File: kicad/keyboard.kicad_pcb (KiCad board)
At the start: 2 copper layers, 266 x 95 mm, 74 parts, among them SW1 SW_MEC_5G, SW10 SW_MEC_5G, SW11 SW_MEC_5G, SW12 SW_MEC_5G, SW13 SW_MEC_5G, SW14 SW_MEC_5G, SW15 SW_MEC_5G, SW16 SW_MEC_5G, SW17 SW_MEC_5G, SW18 SW_MEC_5G, SW19 SW_MEC_5G, SW2 SW_MEC_5G, SW20 SW_MEC_5G, SW21 SW_MEC_5G, SW22 SW_MEC_5G, SW23 SW_MEC_5G, SW24 SW_MEC_5G, SW25 SW_MEC_5G, SW26 SW_MEC_5G, SW27 SW_MEC_5G, SW28 SW_MEC_5G, SW29 SW_MEC_5G, SW3 SW_MEC_5G, SW30 SW_MEC_5G, SW31 SW_MEC_5G, SW32 SW_MEC_5G, SW33 SW_MEC_5G, SW34 SW_MEC_5G, SW35 SW_MEC_5G, SW36 SW_MEC_5G, SW37 SW_MEC_5G, SW38 SW_MEC_5G, SW39 SW_MEC_5G, SW4 SW_MEC_5G, SW40 SW_MEC_5G, SW41 SW_MEC_5G, SW42 SW_MEC_5G, SW43 SW_MEC_5G, SW44 SW_MEC_5G, SW45 SW_MEC_5G, SW46 SW_MEC_5G, SW47 SW_MEC_5G, SW48 SW_MEC_5G, SW49 SW_MEC_5G, SW5 SW_MEC_5G, SW50 SW_MEC_5G, SW51 SW_MEC_5G, SW52 SW_MEC_5G, SW53 SW_MEC_5G, SW54 SW_MEC_5G, SW55 SW_MEC_5G, SW56 SW_MEC_5G, SW57 SW_MEC_5G, SW58 SW_MEC_5G, SW59 SW_MEC_5G, SW6 SW_MEC_5G, SW60 SW_MEC_5G, SW7 SW_MEC_5G, SW8 SW_MEC_5G, SW9 SW_MEC_5G, U1 MCP23017-E/SO, U2 MCP23017-E/SO, U3 MCP23017-E/SO, U4 MCP23017-E/SO

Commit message: Started tracing signals, added jlcpcb settings
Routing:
- net /SW12: track 0.00 -> 11.6 mm
- net /SW16: track 0.00 -> 11.6 mm
- net /SW5: track 0.00 -> 11.6 mm
- net /SW19: track 0.00 -> 11.6 mm
- net /SW2: track 0.00 -> 11.5 mm
- net /SW48: track 0.00 -> 11.5 mm
- net /SW20: track 0.00 -> 11.5 mm
- net /SW4: track 0.00 -> 11.5 mm
- net /SW50: track 0.00 -> 11.5 mm
- net /SW52: track 0.00 -> 11.5 mm
- net /SW60: track 0.00 -> 11.5 mm
- net /SW17: track 0.00 -> 11.5 mm
- net /SW42: track 0.00 -> 11.5 mm
- net /SW56: track 0.00 -> 11.5 mm
- net /SW28: track 0.00 -> 11.4 mm
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
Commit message: wip tracing
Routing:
- net /3v3: track 0.00 -> 93.9 mm, vias 0 -> 4
- net /SW33: track 0.00 -> 12.9 mm
- net /SW29: track 0.00 -> 12.8 mm
- net /SW47: track 0.00 -> 11.9 mm
- net /SW43: track 0.00 -> 11.8 mm
- net /SW35: track 0.00 -> 11.7 mm
- net /SW53: track 0.00 -> 11.4 mm
- net /SW51: track 0.00 -> 11.4 mm
- net /SW49: track 0.00 -> 11.4 mm
- net /SW41: track 0.00 -> 11.4 mm
- net /SW39: track 0.00 -> 11.4 mm
- net /SW37: track 0.00 -> 11.4 mm
- net /SW59: track 0.00 -> 11.4 mm
- net /SW57: track 0.00 -> 11.4 mm
- net /SW55: track 0.00 -> 11.4 mm
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- added copper zone on B.Cu, net /GND

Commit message: WIP tracing
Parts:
- A1: value TINY2040 -> TINY2040-pimoroni-boards
- moved R4 24.4 mm to (207.2, 129.2)
- moved R1 1.18 mm to (222.8, 106.0)
- moved R5 1.16 mm to (227.2, 105.9)
- moved R9 0.26 mm to (227.4, 157.3), turned to -90 degrees
- moved R8 0.24 mm to (207.4, 157.1), turned to -90 degrees
- moved R7 0.12 mm to (222.5, 157.2)
- turned R6 to 90 degrees
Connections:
- U1 pad 21: /SW2 -> /SW4
- U1 pad 22: /SW4 -> /SW2
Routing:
- net /SW23: track 10.9 -> 175.2 mm
- net /SW59: track 11.4 -> 164.7 mm
- net /SW21: track 11.3 -> 158.3 mm
- net /SW34: track 11.4 -> 156.1 mm
- net /SW6: track 11.3 -> 149.4 mm
- net /SW57: track 11.4 -> 147.8 mm
- net /SW11: track 11.3 -> 142.0 mm
- net /SW46: track 11.4 -> 140.5 mm
- net /SW19: track 11.6 -> 140.2 mm
- net /SW36: track 11.4 -> 135.2 mm
- net /SW35: track 11.7 -> 132.0 mm
- net /SW55: track 11.4 -> 131.1 mm
- net /SW8: track 11.4 -> 130.6 mm
- net /SW47: track 11.9 -> 130.4 mm
- net /SW31: track 11.0 -> 124.6 mm
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
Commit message: WIP tracing
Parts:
- moved R4 70.3 mm to (214.6, 59.2)
- moved R1 64.4 mm to (222.3, 41.5)
- moved R5 63.8 mm to (228.8, 42.1)
- moved U1 62.7 mm to (204.1, 54.6)
- moved U2 62.2 mm to (228.5, 55.1)
- moved R6 43.4 mm to (203.8, 200.6)
- moved R8 42.9 mm to (197.3, 198.8)
- moved R7 39.7 mm to (241.1, 192.3)
- moved U3 38.6 mm to (201.6, 184.2)
- moved U4 38.0 mm to (225.6, 183.8)
- moved R9 33.3 mm to (233.2, 190.1)
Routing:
- net /SW59: track 164.7 -> 9.76 mm
- net /SW57: track 147.8 -> 11.4 mm
- net /3v3: track 152.9 -> 27.7 mm, vias 4 -> 0
- net /SW55: track 131.1 -> 11.4 mm
- net /SW47: track 130.4 -> 11.0 mm
- net /SW53: track 113.0 -> 11.4 mm
- net /SW45: track 111.5 -> 11.1 mm
- net /SW29: track 106.9 -> 13.1 mm
- net /SW43: track 93.7 -> 12.4 mm
- net /SW51: track 90.7 -> 11.4 mm
- net /SW27: track 85.6 -> 11.2 mm
- net /SW49: track 73.1 -> 0.00 mm
- net /SW41: track 74.2 -> 11.7 mm
- net /SW17: track 121.0 -> 63.1 mm
- net /SW19: track 140.2 -> 82.9 mm
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
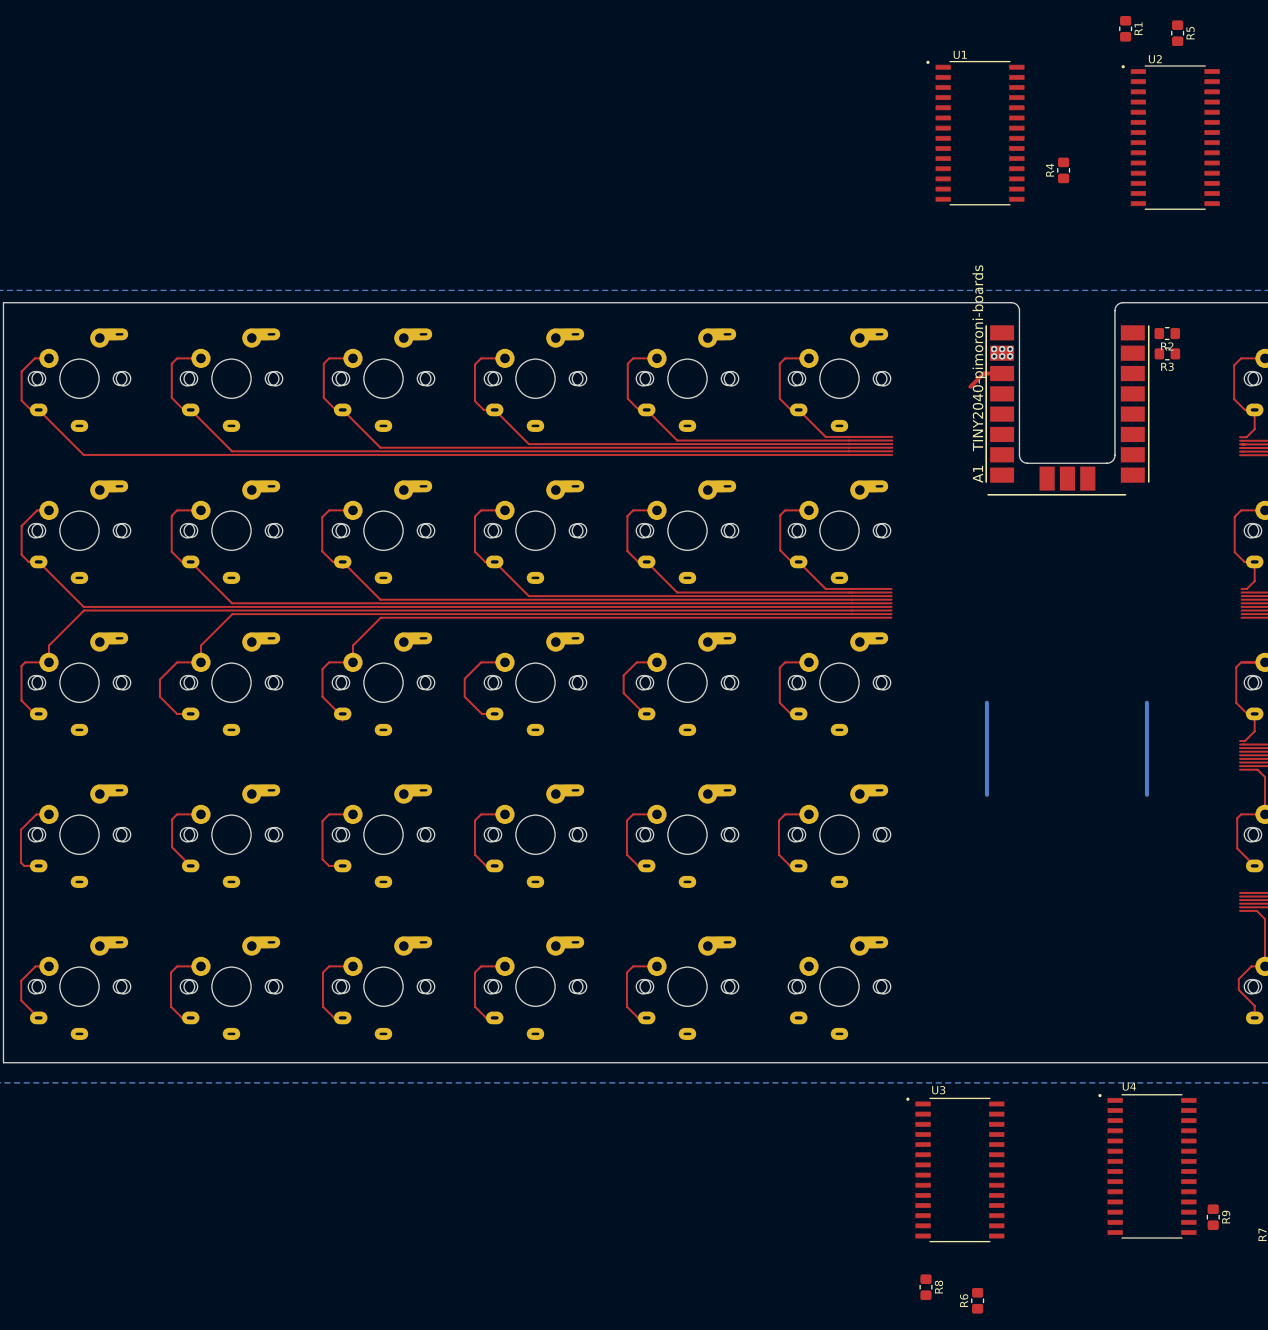
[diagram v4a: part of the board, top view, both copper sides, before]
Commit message: Reordered switch pins and re-traced
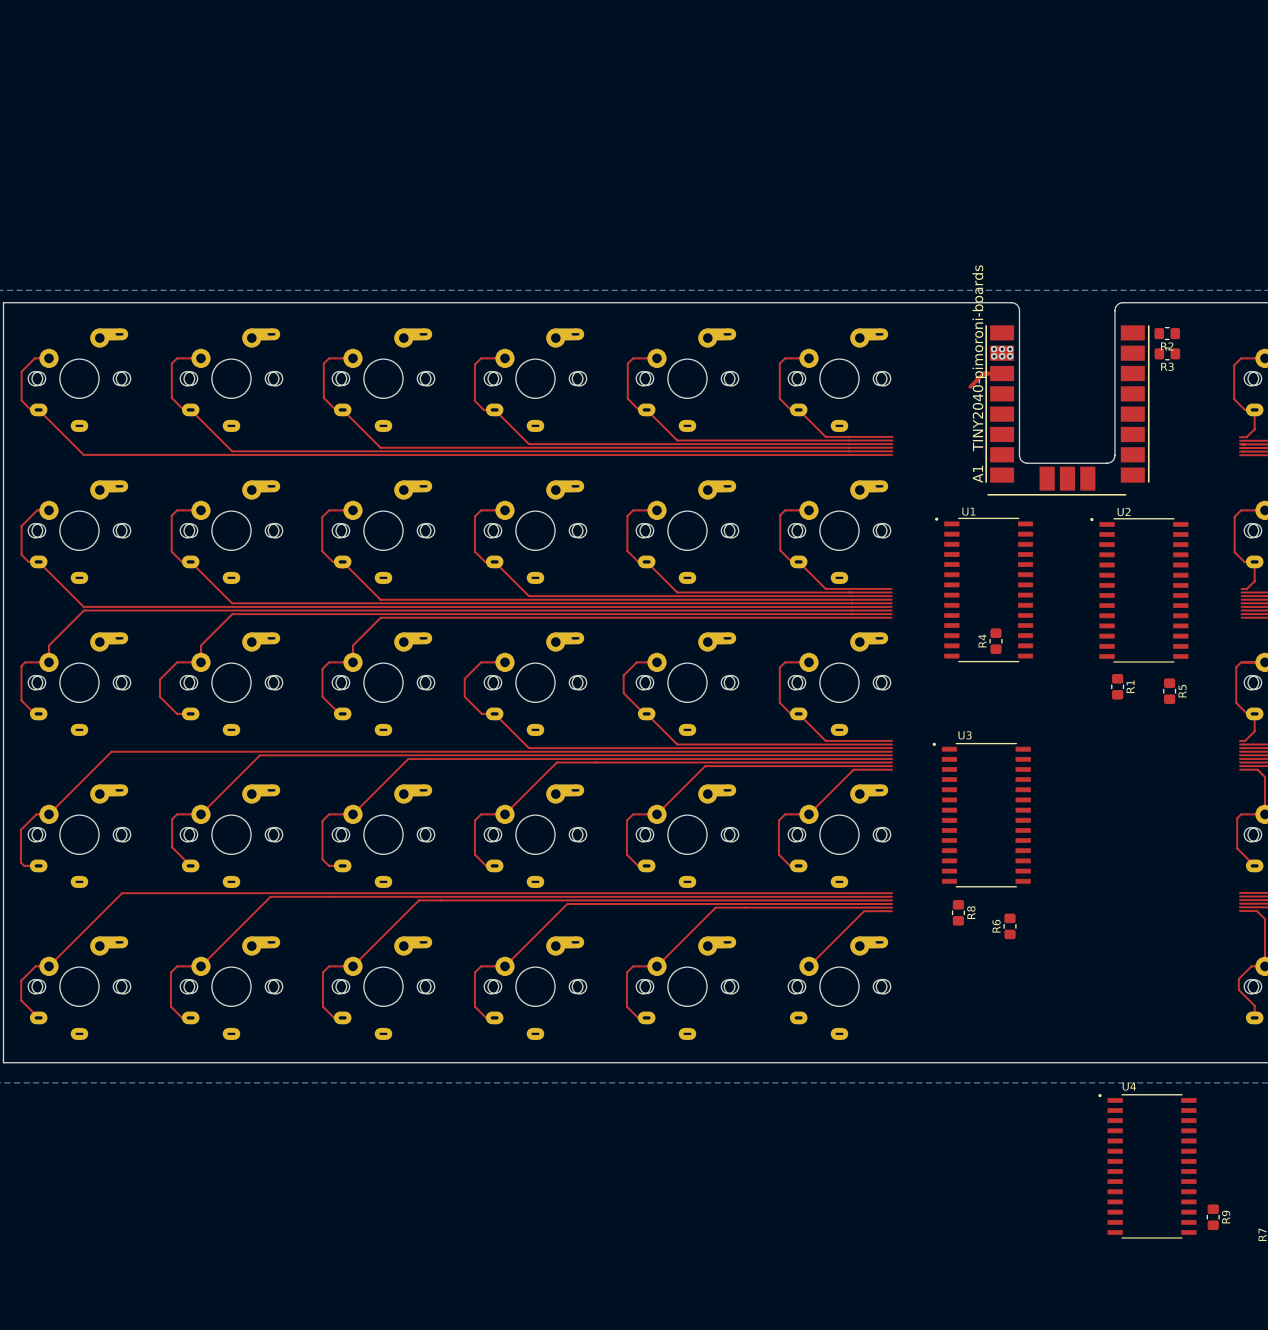
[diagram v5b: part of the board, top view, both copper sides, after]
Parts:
- moved R1 82.3 mm to (221.3, 123.8)
- moved R5 82.3 mm to (227.8, 124.3)
- moved R4 59.5 mm to (206.1, 118.1)
- moved U1 57.1 mm to (205.2, 111.7)
- moved U2 56.7 mm to (224.6, 111.8)
- moved R6 47.0 mm to (207.8, 153.8)
- moved R8 47.0 mm to (201.4, 152.1)
- moved U3 44.5 mm to (204.9, 139.8)
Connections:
- U1 pad 2: /SW3 -> /SW5
- U1 pad 21: /SW4 -> unconnected-(U1-Pad21)
- U1 pad 22: /SW2 -> /SW33
- U1 pad 23: /SW6 -> /SW23
- U1 pad 24: /SW8 -> /SW19
- U1 pad 25: /SW10 -> /SW15
- U1 pad 26: /SW12 -> /SW11
- U1 pad 27: /SW14 -> /SW7
- U1 pad 28: /SW16 -> /SW3
- U1 pad 3: /SW5 -> /SW9
- U1 pad 4: /SW7 -> /SW13
- U1 pad 5: /SW9 -> /SW17
- U1 pad 6: /SW11 -> /SW21
- U1 pad 7: /SW13 -> /SW35
- U1 pad 8: /SW15 -> /SW31
- U2 pad 1: /SW17 -> unconnected-(U2-Pad1)
- U2 pad 2: /SW19 -> unconnected-(U2-Pad2)
- U2 pad 3: /SW21 -> unconnected-(U2-Pad3)
- U2 pad 4: /SW23 -> unconnected-(U2-Pad4)
- U2 pad 5: /SW25 -> unconnected-(U2-Pad5)
- U2 pad 6: /SW27 -> unconnected-(U2-Pad6)
- U2 pad 7: /SW29 -> unconnected-(U2-Pad7)
- U2 pad 8: /SW31 -> unconnected-(U2-Pad8)
- U3 pad 1: /SW33 -> /SW25
- U3 pad 2: /SW35 -> /SW29
- U3 pad 21: /SW34 -> unconnected-(U3-Pad21)
- U3 pad 22: /SW36 -> /SW51
- U3 pad 23: /SW38 -> /SW55
- U3 pad 24: /SW40 -> /SW59
- U3 pad 25: /SW42 -> /SW39
- U3 pad 26: /SW44 -> /SW43
- U3 pad 27: /SW46 -> /SW47
- U3 pad 28: /SW48 -> /SW27
- U3 pad 3: /SW37 -> /SW45
- U3 pad 4: /SW39 -> /SW41
- U3 pad 5: /SW41 -> /SW37
- U3 pad 6: /SW43 -> /SW57
- U3 pad 7: /SW45 -> /SW53
- U3 pad 8: /SW47 -> /SW49
- U4 pad 1: /SW49 -> unconnected-(U4-Pad1)
- U4 pad 2: /SW51 -> unconnected-(U4-Pad2)
- U4 pad 3: /SW53 -> unconnected-(U4-Pad3)
- U4 pad 4: /SW55 -> unconnected-(U4-Pad4)
- U4 pad 5: /SW57 -> unconnected-(U4-Pad5)
- U4 pad 6: /SW59 -> unconnected-(U4-Pad6)
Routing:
- net /SW59: track 9.76 -> 118.9 mm
- net /SW47: track 11.0 -> 119.7 mm
- net /SW57: track 11.4 -> 101.4 mm
- net /SW45: track 11.1 -> 100.5 mm
- net /SW55: track 11.4 -> 82.2 mm
- net /SW43: track 12.4 -> 82.6 mm
- net /SW53: track 11.4 -> 63.0 mm
- net /SW29: track 13.1 -> 64.5 mm
- net /SW41: track 11.7 -> 62.8 mm
- net /SW51: track 11.4 -> 43.8 mm
- net /SW27: track 11.2 -> 43.4 mm
- net /SW39: track 11.4 -> 43.3 mm
- net /3v3: track 27.7 -> 4.65 mm
- net /SW49: track 0.00 -> 13.2 mm
- net /SW25: track 11.3 -> 24.3 mm
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
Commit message: Reordered switch pins and re-traced
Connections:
- U2 pad 1: unconnected-(U2-Pad1) -> /SW14
- U2 pad 2: unconnected-(U2-Pad2) -> /SW10
- U2 pad 21: /SW18 -> /SW44
- U2 pad 22: /SW20 -> /SW40
- U2 pad 23: /SW22 -> /SW36
- U2 pad 24: /SW24 -> /SW20
- U2 pad 25: /SW26 -> /SW24
- U2 pad 26: /SW28 -> /SW8
- U2 pad 27: /SW30 -> /SW12
- U2 pad 28: /SW32 -> /SW16
- U2 pad 3: unconnected-(U2-Pad3) -> /SW6
- U2 pad 4: unconnected-(U2-Pad4) -> /SW22
- U2 pad 5: unconnected-(U2-Pad5) -> /SW34
- U2 pad 6: unconnected-(U2-Pad6) -> /SW38
- U2 pad 7: unconnected-(U2-Pad7) -> /SW42
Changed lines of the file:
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@@
   (net 97 "unconnected-(U4-Pad8)")
   (net 98 "unconnected-(U4-Pad7)")
-  (net 99 "unconnected-(U2-Pad1)")
-  (net 100 "unconnected-(U2-Pad2)")
-  (net 101 "unconnected-(U1-Pad21)")
-  (net 102 "unconnected-(U2-Pad3)")
-  (net 103 "unconnected-(U2-Pad4)")
-  (net 104 "unconnected-(U2-Pad8)")
-  (net 105 "unconnected-(U2-Pad5)")
-  (net 106 "unconnected-(U2-Pad6)")
-  (net 107 "unconnected-(U2-Pad7)")
-  (net 108 "unconnected-(U3-Pad21)")
-  (net 109 "unconnected-(U4-Pad1)")
-  (net 110 "unconnected-(U4-Pad2)")
-  (net 111 "unconnected-(U4-Pad3)")
-  (net 112 "unconnected-(U4-Pad4)")
-  (net 113 "unconnected-(U4-Pad5)")
-  (net 114 "unconnected-(U4-Pad6)")
+  (net 99 "unconnected-(U1-Pad21)")
+  (net 100 "unconnected-(U2-Pad8)")
+  (net 101 "unconnected-(U3-Pad21)")
+  (net 102 "unconnected-(U4-Pad1)")
+  (net 103 "unconnected-(U4-Pad2)")
+  (net 104 "unconnected-(U4-Pad3)")
+  (net 105 "unconnected-(U4-Pad4)")
+  (net 106 "unconnected-(U4-Pad5)")
+  (net 107 "unconnected-(U4-Pad6)")
   (footprint "footprints:CherryMX_ChocV2_1u" (layer "F.Cu")
     (at 338.532 85.29)
@@
       (net 91 "unconnected-(U3-Pad20)") (pinfunction "INTA") (pintype "output+no_connect"))
     (pad "21" smd roundrect locked (at 4.605 0.635) (size 1.9 0.6) (layers "F.Cu" "F.Paste" "F.Mask") (roundrect_rratio 0.07)
-      (net 108 "unconnected-(U3-Pad21)") (pinfunction "GPA0") (pintype "bidirectional"))
+      (net 101 "unconnected-(U3-Pad21)") (pinfunction "GPA0") (pintype "bidirectional"))
     (pad "22" smd roundrect locked (at 4.605 -0.635) (size 1.9 0.6) (layers "F.Cu" "F.Paste" "F.Mask") (roundrect_rratio 0.07)
       (net 77 "/SW51") (pinfunction "GPA1") (pintype "bidirectional"))
@@
     (fp_circle (center -6.505 -8.855) (end -6.405 -8.855) (layer "F.Fab") (width 0.2) (fill none))
     (pad "1" smd roundrect locked (at -4.605 -8.255) (size 1.9 0.6) (layers "F.Cu" "F.Paste" "F.Mask") (roundrect_rratio 0.07)
-      (net 109 "unconnected-(U4-Pad1)") (pinfunction "GPB0") (pintype "bidirectional"))
+      (net 102 "unconnected-(U4-Pad1)") (pinfunction "GPB0") (pintype "bidirectional"))
     (pad "2" smd roundrect locked (at -4.605 -6.985) (size 1.9 0.6) (layers "F.Cu" "F.Paste" "F.Mask") (roundrect_rratio 0.07)
-      (net 110 "unconnected-(U4-Pad2)") (pinfunction "GPB1") (pintype "bidirectional"))
+      (net 103 "unconnected-(U4-Pad2)") (pinfunction "GPB1") (pintype "bidirectional"))
     (pad "3" smd roundrect locked (at -4.605 -5.715) (size 1.9 0.6) (layers "F.Cu" "F.Paste" "F.Mask") (roundrect_rratio 0.07)
-      (net 111 "unconnected-(U4-Pad3)") (pinfunction "GPB2") (pintype "bidirectional"))
+      (net 104 "unconnected-(U4-Pad3)") (pinfunction "GPB2") (pintype "bidirectional"))
     (pad "4" smd roundrect locked (at -4.605 -4.445) (size 1.9 0.6) (layers "F.Cu" "F.Paste" "F.Mask") (roundrect_rratio 0.07)
-      (net 112 "unconnected-(U4-Pad4)") (pinfunction "GPB3") (pintype "bidirectional"))
+      (net 105 "unconnected-(U4-Pad4)") (pinfunction "GPB3") (pintype "bidirectional"))
     (pad "5" smd roundrect locked (at -4.605 -3.175) (size 1.9 0.6) (layers "F.Cu" "F.Paste" "F.Mask") (roundrect_rratio 0.07)
-      (net 113 "unconnected-(U4-Pad5)") (pinfunction "GPB4") (pintype "bidirectional"))
+      (net 106 "unconnected-(U4-Pad5)") (pinfunction "GPB4") (pintype "bidirectional"))
     (pad "6" smd roundrect locked (at -4.605 -1.905) (size 1.9 0.6) (layers "F.Cu" "F.Paste" "F.Mask") (roundrect_rratio 0.07)
-      (net 114 "unconnected-(U4-Pad6)") (pinfunction "GPB5") (pintype "bidirectional"))
+      (net 107 "unconnected-(U4-Pad6)") (pinfunction "GPB5") (pintype "bidirectional"))
     (pad "7" smd roundrect locked (at -4.605 -0.635) (size 1.9 0.6) (layers "F.Cu" "F.Paste" "F.Mask") (roundrect_rratio 0.07)
       (net 98 "unconnected-(U4-Pad7)") (pinfunction "GPB6") (pintype "bidirectional+no_connect"))
@@
       (net 87 "unconnected-(U1-Pad20)") (pinfunction "INTA") (pintype "output+no_connect"))
     (pad "21" smd roundrect locked (at 4.605 0.635) (size 1.9 0.6) (layers "F.Cu" "F.Paste" "F.Mask") (roundrect_rratio 0.07)
-      (net 101 "unconnected-(U1-Pad21)") (pinfunction "GPA0") (pintype "bidirectional"))
+      (net 99 "unconnected-(U1-Pad21)") (pinfunction "GPA0") (pintype "bidirectional"))
     (pad "22" smd roundrect locked (at 4.605 -0.635) (size 1.9 0.6) (layers "F.Cu" "F.Paste" "F.Mask") (roundrect_rratio 0.07)
       (net 59 "/SW33") (pinfunction "GPA1") (pintype "bidirectional"))
@@
     (fp_circle (center -6.505 -8.855) (end -6.405 -8.855) (layer "F.Fab") (width 0.2) (fill none))
     (pad "1" smd roundrect locked (at -4.605 -8.255) (size 1.9 0.6) (layers "F.Cu" "F.Paste" "F.Mask") (roundrect_rratio 0.07)
-      (net 99 "unconnected-(U2-Pad1)") (pinfunction "GPB0") (pintype "bidirectional"))
+      (net 40 "/SW14") (pinfunction "GPB0") (pintype "bidirectional"))
     (pad "2" smd roundrect locked (at -4.605 -6.985) (size 1.9 0.6) (layers "F.Cu" "F.Paste" "F.Mask") (roundrect_rratio 0.07)
-      (net 100 "unconnected-(U2-Pad2)") (pinfunction "GPB1") (pintype "bidirectional"))
+      (net 36 "/SW10") (pinfunction "GPB1") (pintype "bidirectional"))
     (pad "3" smd roundrect locked (at -4.605 -5.715) (size 1.9 0.6) (layers "F.Cu" "F.Paste" "F.Mask") (roundrect_rratio 0.07)
-      (net 102 "unconnected-(U2-Pad3)") (pinfunction "GPB2") (pintype "bidirectional"))
+      (net 32 "/SW6") (pinfunction "GPB2") (pintype "bidirectional"))
     (pad "4" smd roundrect locked (at -4.605 -4.445) (size 1.9 0.6) (layers "F.Cu" "F.Paste" "F.Mask") (roundrect_rratio 0.07)
-      (net 103 "unconnected-(U2-Pad4)") (pinfunction "GPB3") (pintype "bidirectional"))
+      (net 48 "/SW22") (pinfunction "GPB3") (pintype "bidirectional"))
     (pad "5" smd roundrect locked (at -4.605 -3.175) (size 1.9 0.6) (layers "F.Cu" "F.Paste" "F.Mask") (roundrect_rratio 0.07)
-      (net 105 "unconnected-(U2-Pad5)") (pinfunction "GPB4") (pintype "bidirectional"))
+      (net 60 "/SW34") (pinfunction "GPB4") (pintype "bidirectional"))
     (pad "6" smd roundrect locked (at -4.605 -1.905) (size 1.9 0.6) (layers "F.Cu" "F.Paste" "F.Mask") (roundrect_rratio 0.07)
-      (net 106 "unconnected-(U2-Pad6)") (pinfunction "GPB5") (pintype "bidirectional"))
+      (net 64 "/SW38") (pinfunction "GPB5") (pintype "bidirectional"))
     (pad "7" smd roundrect locked (at -4.605 -0.635) (size 1.9 0.6) (layers "F.Cu" "F.Paste" "F.Mask") (roundrect_rratio 0.07)
-      (net 107 "unconnected-(U2-Pad7)") (pinfunction "GPB6") (pintype "bidirectional"))
+      (net 68 "/SW42") (pinfunction "GPB6") (pintype "bidirectional"))
     (pad "8" smd roundrect locked (at -4.605 0.635) (size 1.9 0.6) (layers "F.Cu" "F.Paste" "F.Mask") (roundrect_rratio 0.07)
-      (net 104 "unconnected-(U2-Pad8)") (pinfunction "GPB7") (pintype "bidirectional"))
+      (net 100 "unconnected-(U2-Pad8)") (pinfunction "GPB7") (pintype "bidirectional"))
     (pad "9" smd roundrect locked (at -4.605 1.905) (size 1.9 0.6) (layers "F.Cu" "F.Paste" "F.Mask") (roundrect_rratio 0.07)
       (net 5 "/3v3") (pinfunction "VDD") (pintype "power_in"))
@@
       (net 89 "unconnected-(U2-Pad20)") (pinfunction "INTA") (pintype "output+no_connect"))
     (pad "21" smd roundrect locked (at 4.605 0.635) (size 1.9 0.6) (layers "F.Cu" "F.Paste" "F.Mask") (roundrect_rratio 0.07)
-      (net 44 "/SW18") (pinfunction "GPA0") (pintype "bidirectional"))
+      (net 70 "/SW44") (pinfunction "GPA0") (pintype "bidirectional"))
     (pad "22" smd roundrect locked (at 4.605 -0.635) (size 1.9 0.6) (layers "F.Cu" "F.Paste" "F.Mask") (roundrect_rratio 0.07)
-      (net 46 "/SW20") (pinfunction "GPA1") (pintype "bidirectional"))
+      (net 66 "/SW40") (pinfunction "GPA1") (pintype "bidirectional"))
     (pad "23" smd roundrect locked (at 4.605 -1.905) (size 1.9 0.6) (layers "F.Cu" "F.Paste" "F.Mask") (roundrect_rratio 0.07)
-      (net 48 "/SW22") (pinfunction "GPA2") (pintype "bidirectional"))
+      (net 62 "/SW36") (pinfunction "GPA2") (pintype "bidirectional"))
     (pad "24" smd roundrect locked (at 4.605 -3.175) (size 1.9 0.6) (layers "F.Cu" "F.Paste" "F.Mask") (roundrect_rratio 0.07)
-      (net 50 "/SW24") (pinfunction "GPA3") (pintype "bidirectional"))
+      (net 46 "/SW20") (pinfunction "GPA3") (pintype "bidirectional"))
     (pad "25" smd roundrect locked (at 4.605 -4.445) (size 1.9 0.6) (layers "F.Cu" "F.Paste" "F.Mask") (roundrect_rratio 0.07)
-      (net 52 "/SW26") (pinfunction "GPA4") (pintype "bidirectional"))
+      (net 50 "/SW24") (pinfunction "GPA4") (pintype "bidirectional"))
     (pad "26" smd roundrect locked (at 4.605 -5.715) (size 1.9 0.6) (layers "F.Cu" "F.Paste" "F.Mask") (roundrect_rratio 0.07)
-      (net 54 "/SW28") (pinfunction "GPA5") (pintype "bidirectional"))
+      (net 34 "/SW8") (pinfunction "GPA5") (pintype "bidirectional"))
     (pad "27" smd roundrect locked (at 4.605 -6.985) (size 1.9 0.6) (layers "F.Cu" "F.Paste" "F.Mask") (roundrect_rratio 0.07)
-      (net 56 "/SW30") (pinfunction "GPA6") (pintype "bidirectional"))
+      (net 38 "/SW12") (pinfunction "GPA6") (pintype "bidirectional"))
     (pad "28" smd roundrect locked (at 4.605 -8.255) (size 1.9 0.6) (layers "F.Cu" "F.Paste" "F.Mask") (roundrect_rratio 0.07)
-      (net 58 "/SW32") (pinfunction "GPA7") (pintype "bidirectional"))
-  )
-  (footprint "footprints:CherryMX_ChocV2_1u" (layer "F.Cu")
+      (net 42 "/SW16") (pinfunction "GPA7") (pintype "bidirectional"))
+  )
+  (footprint "footprints:CherryMX_ChocV2_1u" (layer "F.Cu")
